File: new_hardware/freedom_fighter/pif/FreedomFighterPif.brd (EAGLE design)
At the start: 160 x 100 mm, 34 parts, among them U1 PIA6821, U10 74LS74D, U11 74LS138D, U12 74LS125D, U2 HM6116P-A, U4 HD68A09EP, U5 74LS74D, U6 74LS245DW, U7 74LS10D, U9 74LS04D, X1 CRYSTAL OSC

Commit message: Essentially finished schematic, started laying out PCB
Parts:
- removed IC1: (no value), memory:DIL28
- removed X1: CRYSTAL OSC, crystal:TC46
- added C1, C10, C11, C12, C13, C2, C3, C4, C5, C7, C8: 0.1uF, SparkFun:1206
- added JP1, JP4: (no value), pinhead:1X20
- added JP2, JP5, JP6: (no value), pinhead:1X08
- added JP3: (no value), pinhead:1X02
- added JP7, JP8: (no value), pinhead:1X07
- added U$1: OSCILLATOR-SMT4, mpo:SMT4-7MMX5MM
- added U3: (no value), memory:DIL28
- L1: device rcl:TJ8-U2 -> SparkFun:INDUCTOR-1206
- moved R11 238.3 mm to (63.5, 33.0)
- moved R12 228.6 mm to (54.6, 21.6)
- moved C15 218.0 mm to (15.2, 27.9), turned to 270 degrees
- moved C100 214.4 mm to (129.5, 77.5), turned to 90 degrees
- moved R4 210.5 mm to (142.2, 95.2)
- moved R5 203.5 mm to (135.9, 95.2)
- moved R6 196.4 mm to (129.5, 95.2)
- moved L1 187.0 mm to (15.2, 17.8)
- moved R10 168.9 mm to (63.5, 38.1), turned to 180 degrees
- moved U7 168.0 mm to (148.6, 63.5), turned to 270 degrees
- moved C14 164.2 mm to (14.0, 22.9)
- moved U12 160.2 mm to (148.6, 38.1), turned to 270 degrees
- moved U11 154.6 mm to (135.9, 38.1), turned to 270 degrees
- moved C9 150.3 mm to (14.0, 12.7), turned to 180 degrees
- moved U6 149.4 mm to (135.9, 62.2), turned to 270 degrees
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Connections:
- net !ENABLE_DAVDAK: now also JP6.3
- net !ENABLE_PIA: now also JP6.6
- net !ENABLE_RAM: now also JP6.2
- net !ENABLE_ROM: now also U3.20; no longer IC1.20
- net !ENABLE_ROM_C_TO_D: now also JP6.8
- net !ENABLE_ROM_E_TO_F: now also JP5.7
- net !ENABLE_VP931_DATA: now also JP6.5, JP8.6
- net !HALT: now also JP4.1
- net !IRQ: now also JP1.3
- net !IRQA/FIRQ: now also JP1.4
- net !IRQB/NMI: now also JP1.2
- net !RESET: now also JP4.4
- net 4MHZ: now also U$1.3; no longer X1.8
- net A0: now also JP1.8, U3.10; no longer IC1.10
- net A1: now also JP1.9, U3.9; no longer IC1.9
- net A10: now also JP1.18, U3.21; no longer IC1.21
- net A11: now also JP1.19, U3.23; no longer IC1.23
- net A12: now also JP1.20, U3.2; no longer IC1.2
- net A13: now also JP4.20, U3.26; no longer IC1.26
- net A14: now also JP4.19
- net A15: now also JP4.18
- net A2: now also JP1.10, U3.8; no longer IC1.8
- net A3: now also JP1.11, U3.7; no longer IC1.7
- net A4: now also JP1.12, U3.6; no longer IC1.6
- net A5: now also JP1.13, U3.5; no longer IC1.5
- net A6: now also JP1.14, U3.4; no longer IC1.4
- net A7: now also JP1.15, U3.3; no longer IC1.3
- net A8: now also JP1.16, U3.25; no longer IC1.25
- net A9: now also JP1.17, U3.24; no longer IC1.24
- net D0: now also JP4.10, U3.19; no longer IC1.19
- net D1: now also JP4.11, U3.18; no longer IC1.18
- net D2: now also JP4.12, U3.11; no longer IC1.11
- net D3: now also JP4.13, U3.16; no longer IC1.16
- net D4: now also JP4.14, U3.15; no longer IC1.15
- net D5: now also JP4.15, U3.13; no longer IC1.13
- net D6: now also JP4.16, U3.12; no longer IC1.12
- net D7: now also JP4.17, U3.17; no longer IC1.17
- net E: now also JP4.7
- net ENABLE_VP931_DATA: now also JP8.7
- net EVEN/!ODD: now also JP7.3
- net GND: now also C1.2, C10.2, C11.2, C12.2, C13.2, C2.2, C3.2, C4.2, C5.2, C7.2, C8.2, JP1.1, JP5.8, JP7.7, U$1.2, U3.14, U3.22; no longer IC1.14, IC1.22, X1.7
- net HAND1: now also JP3.1
- net HAND2: now also JP3.2
- net N$8: now also L1.P$1; no longer L1.1
- net PA0: now also JP2.1
- net PA1: now also JP2.2
- net PA2: now also JP2.3
- net PA3: now also JP2.4
- net PA4: now also JP2.5
- net PA5: now also JP2.6
- net PA6: now also JP2.7
- net PA7: now also JP2.8
- net Q: now also JP4.6
- net R/!W: now also JP4.9, JP7.1
- net VCC: now also C1.1, C10.1, C11.1, C12.1, C13.1, C2.1, C3.1, C4.1, C5.1, C7.1, C8.1, JP1.7, JP6.1, JP8.1, L1.P$2, U$1.1, U$1.4, U3.1, U3.27, U3.28; no longer IC1.1, IC1.27, IC1.28, L1.2, X1.14
- net W/!R: now also JP7.2
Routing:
- net VCC: track 67.4 -> 149.4 mm
- net EVEN/!ODD: track 115.4 -> 35.9 mm, vias 1 -> 0
- net D2: track 0.00 -> 23.3 mm, vias 0 -> 1
- net D1: track 0.00 -> 19.8 mm, vias 0 -> 1
- net D5: track 0.00 -> 19.6 mm
- net D7: track 0.00 -> 19.4 mm
- net D6: track 0.00 -> 19.2 mm
- net D4: track 0.00 -> 18.3 mm
- net D3: track 0.00 -> 17.1 mm
- net D0: track 0.00 -> 16.8 mm, vias 0 -> 1
- net HAND2: track 54.1 -> 70.4 mm
- net HAND1: track 57.3 -> 73.4 mm
- net N$8: track 0.00 -> 12.7 mm
- net ENABLE_VP931_DATA: track 0.00 -> 6.05 mm
- net R/!W: track 0.00 -> 5.94 mm
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
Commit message: Schematic is "final", but I will be removing stuff from it to make the board so I am saving it
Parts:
- removed C100: Unknown value, SparkFun:1206
- removed C9: 0.001uF, SparkFun:1206
- added R100: 680, SparkFun:1206
- moved DB1 71.5 mm to (43.2, 6.35)
- moved C1 51.1 mm to (22.9, 44.5), turned to 90 degrees
- moved R12 34.2 mm to (80.0, 44.5), turned to 90 degrees
- moved C15 5.08 mm to (15.2, 33.0)
- moved U2 3.81 mm to (58.4, 68.6)
- moved J1 2.54 mm to (5.08, 20.3)
- moved C14 1.80 mm to (12.7, 24.1), turned to 270 degrees
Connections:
- net E: now also R100.2; no longer C100.2
- net GND: no longer C9.1
- net N$8: now also C14.2; no longer C9.2
- net VCC: now also R100.1; no longer C100.1, C14.2
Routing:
- net !RESET: track 0.00 -> 96.1 mm, vias 0 -> 5
- net W/!R: track 5.37 -> 71.6 mm, vias 0 -> 2
- net R/!W: track 5.94 -> 68.8 mm, vias 0 -> 3
- net EVEN/!ODD: track 35.9 -> 76.0 mm, vias 0 -> 1
- net A0: track 0.00 -> 30.3 mm, vias 0 -> 2
- net A1: track 0.00 -> 28.7 mm, vias 0 -> 2
- net D6: track 19.2 -> 40.6 mm, vias 0 -> 2
- net D7: track 19.4 -> 38.3 mm, vias 0 -> 1
- net A10: track 0.00 -> 13.3 mm, vias 0 -> 1
- net !ENABLE_RAM: track 0.00 -> 13.0 mm, vias 0 -> 1
- net D0: track 16.8 -> 7.01 mm
- net VCC: track 149.4 -> 155.0 mm, vias 3 -> 5
- net D5: track 19.6 -> 23.4 mm
- net D4: track 18.3 -> 22.1 mm
- net D3: track 17.1 -> 20.9 mm
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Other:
- board size 160 x 100 mm -> 160 x 114.3 mm

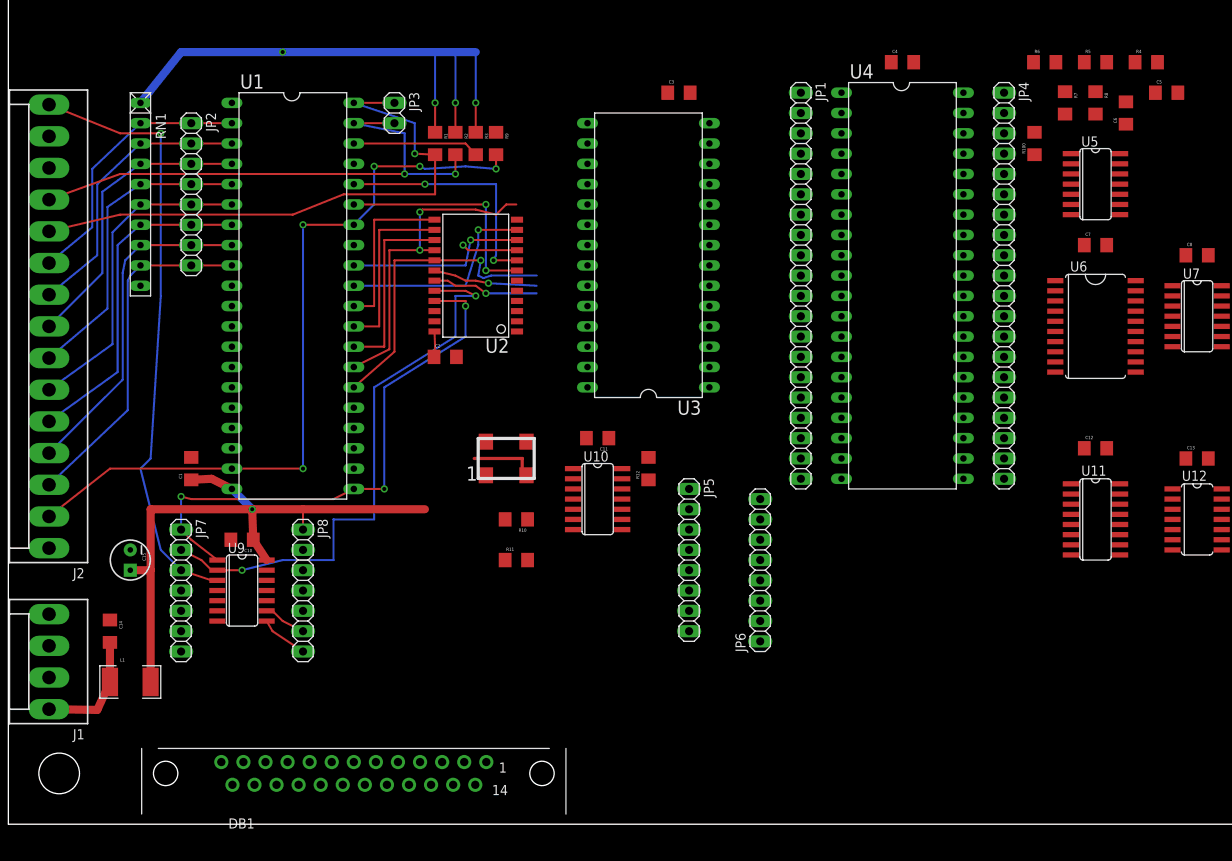
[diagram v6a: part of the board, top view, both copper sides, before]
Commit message: completed about half of the routing.  I'd say the hard part is done.
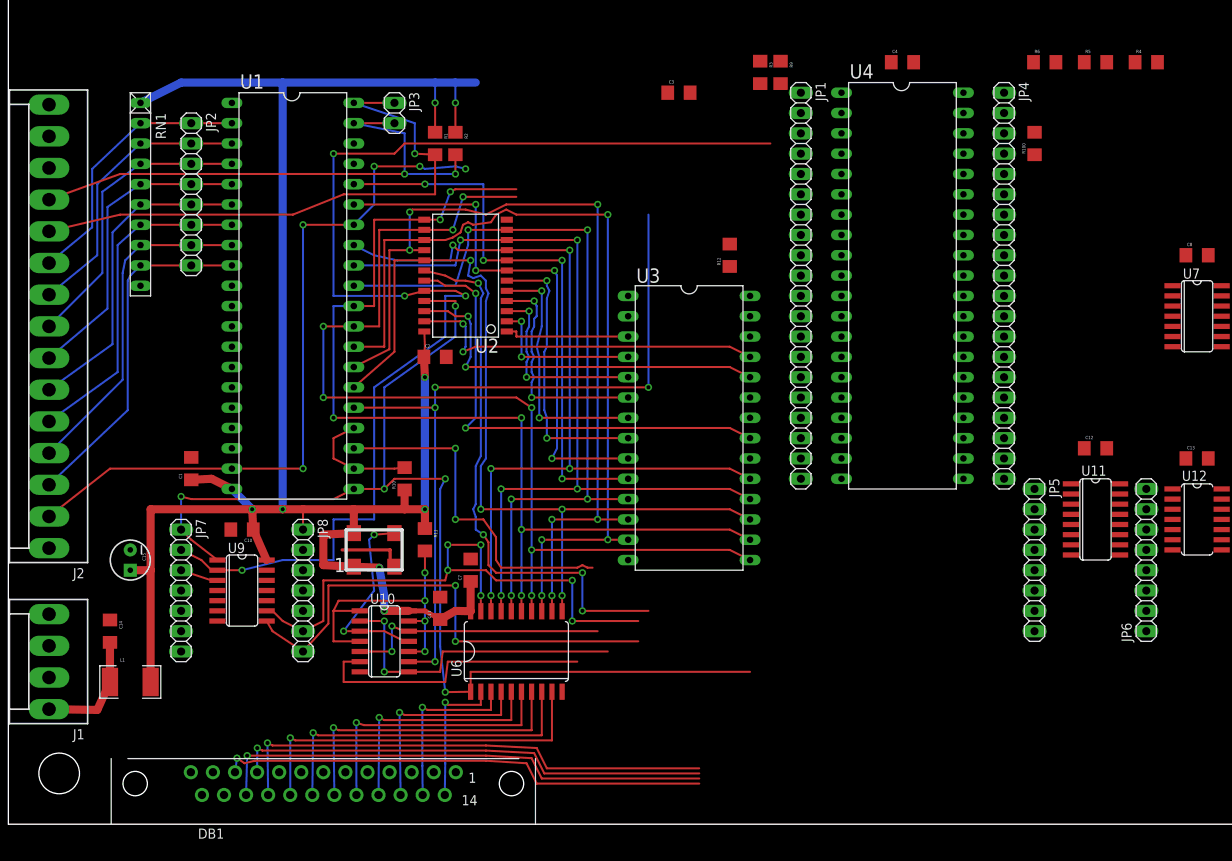
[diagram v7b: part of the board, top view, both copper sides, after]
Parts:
- removed C5: 0.1uF, SparkFun:1206
- removed C6: Not Installed, SparkFun:1206
- removed R7, R8: 4.7k, SparkFun:1206
- removed U5: 74LS74D, 74xx-us:SO14
- moved C7 88.0 mm to (57.8, 31.8), turned to 90 degrees
- moved U6 83.0 mm to (63.5, 21.6), turned to 0 degrees
- moved JP6 48.3 mm to (142.2, 33.0)
- moved JP5 43.2 mm to (128.3, 33.0)
- moved R3 36.7 mm to (94.0, 94.0)
- moved R9 36.7 mm to (96.5, 94.0)
- moved U10 32.1 mm to (47.0, 22.9)
- moved C11 29.0 mm to (54.0, 27.0), turned to 90 degrees
- moved R12 28.5 mm to (90.2, 71.1)
- moved U3 22.2 mm to (85.1, 49.5), turned to 270 degrees
- moved U$1 20.1 mm to (45.7, 34.3)
- moved R10 14.9 mm to (49.5, 43.2), turned to 90 degrees
- moved R11 11.7 mm to (52.1, 35.6), turned to 270 degrees
- moved DB1 4.02 mm to (39.4, 5.08)
- moved U2 1.27 mm to (57.1, 68.6)
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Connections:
- removed net !IRQA/FIRQ: JP1.4, R3.2, U1.38, U4.4
- removed net !IRQB/NMI: JP1.2, R5.2, U1.37, U4.2
- removed net 4MS: C6.1, J2.13, R8.2, U5.11
- removed net N$1: R7.2, U5.1, U5.13, U5.4
- removed net N$2: U5.12, U5.6
- new net !FIRQ: JP1.4, R3.2, U4.4
- new net !NMI: JP1.2, R5.2, U4.2
- net !IRQ: no longer U5.9
- net D0: no longer U5.2
- net EVEN/!ODD: no longer J2.15, U9.3
- net GND: no longer C5.2, C6.2, U5.10, U5.7
- net VCC: no longer C5.1, R7.1, R8.1, U5.14
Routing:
- net D3: track 20.9 -> 126.7 mm, vias 0 -> 6
- net D4: track 22.1 -> 127.6 mm, vias 0 -> 7
- net D0: track 7.01 -> 107.1 mm, vias 1 -> 5
- net E: track 0.00 -> 96.0 mm, vias 0 -> 4
- net VCC: track 155.0 -> 250.1 mm, vias 5 -> 8
- net D1: track 23.0 -> 108.4 mm, vias 1 -> 5
- net D5: track 23.4 -> 107.4 mm, vias 0 -> 4
- net W/!R: track 71.6 -> 154.9 mm, vias 2 -> 4
- net R/!W: track 68.8 -> 143.4 mm, vias 3 -> 5
- net EVEN/!ODD: track 76.0 -> 4.02 mm, vias 1 -> 0
- net D2: track 26.0 -> 97.1 mm, vias 1 -> 5
- net D6: track 40.6 -> 110.9 mm, vias 2 -> 6
- net D7: track 38.3 -> 107.8 mm, vias 1 -> 4
- net !ENABLE_VP931_DATA: track 5.37 -> 74.9 mm, vias 0 -> 6
- net VP931_DAK: track 0.00 -> 63.0 mm, vias 0 -> 1
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
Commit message: 3/4 of the way finished, about to add ground plane
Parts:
- JP5: device pinhead:1X08 -> pinhead:1X02
- moved C8 82.6 mm to (77.5, 29.2), turned to 180 degrees
- moved U7 78.6 mm to (83.8, 19.1), turned to 0 degrees
- moved JP5 40.7 mm to (96.5, 7.62), turned to 180 degrees
- moved U11 39.9 mm to (101.6, 17.8)
- moved JP6 38.1 mm to (109.2, 14.0)
- moved U12 38.1 mm to (118.1, 15.2)
- moved C3 20.5 mm to (86.4, 71.1)
- moved JP4 16.5 mm to (130.8, 52.1)
- moved JP1 16.5 mm to (105.4, 52.1)
- moved U4 16.5 mm to (118.1, 52.1)
- moved R12 2.84 mm to (92.7, 69.8), turned to 180 degrees
- moved C12 2.54 mm to (138.4, 47.0)
- moved C13 2.54 mm to (151.1, 45.7)
- moved U3 1.27 mm to (86.4, 49.5)
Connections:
- net !ENABLE_ROM_E_TO_F: now also JP5.1; no longer JP5.7
- net GND: now also JP5.2; no longer JP5.8
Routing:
- net VCC: track 250.1 -> 384.2 mm, vias 8 -> 11
- net Q: track 33.0 -> 139.2 mm, vias 2 -> 10
- net E: track 96.0 -> 181.6 mm, vias 4 -> 7
- net D2: track 97.1 -> 179.4 mm, vias 5 -> 8
- net A13: track 0.00 -> 70.9 mm, vias 0 -> 1
- net A12: track 0.00 -> 67.3 mm, vias 0 -> 2
- net D5: track 107.4 -> 167.6 mm, vias 4 -> 6
- net A0: track 71.1 -> 127.6 mm, vias 4 -> 5
- net D6: track 110.9 -> 166.0 mm, vias 6 -> 8
- net A7: track 15.8 -> 70.2 mm, vias 0 -> 2
- net A6: track 19.6 -> 68.9 mm, vias 2 -> 4
- net D4: track 127.6 -> 176.6 mm, vias 7 -> 9
- net W/!R: track 154.9 -> 203.4 mm, vias 4 -> 6
- net D1: track 108.4 -> 155.9 mm, vias 5 -> 7
- net D0: track 107.1 -> 154.3 mm, vias 5 -> 7
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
